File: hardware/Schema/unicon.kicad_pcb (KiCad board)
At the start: 2 copper layers, 31 x 45 mm, 72 parts, among them J1 PROG, J2 PWR, J3 SideA, J4 SideB, U1 LM340MP-5.0, U2 SIP21106-3.3, U3 STM32F051C8Tx, U4 AT24C16, Y1 8MHz, Y2 32768 Hz

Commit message: pcb paruosimas, schemos pataisymai
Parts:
- removed R22, R23: 47R, resistors:R_0805
- removed the REF** at (99.4, 113.2)
- added REF**: SolderWirePad_single_0-8mmDrill, Wire_Pads:SolderWirePad_single_0-8mmDrill, F.Cu at (107.0, 104.3)
- added REF**: Pin_Header_Straight_1x20_Pitch2.54mm, Pin_Headers:Pin_Header_Straight_1x20_Pitch2.54mm, F.Cu at (88.2, 154.0)
- added REF**: SolderWirePad_single_0-8mmDrill, Wire_Pads:SolderWirePad_single_0-8mmDrill, F.Cu at (99.8, 119.1)
- added REF**: SolderWirePad_single_0-8mmDrill, Wire_Pads:SolderWirePad_single_0-8mmDrill, F.Cu at (102.5, 124.8)
- added REF**: SolderWirePad_single_0-8mmDrill, Wire_Pads:SolderWirePad_single_0-8mmDrill, F.Cu at (107.8, 122.0)
- added REF**: SolderWirePad_single_0-8mmDrill, Wire_Pads:SolderWirePad_single_0-8mmDrill, F.Cu at (114.4, 118.9)
- added REF**: SolderWirePad_single_0-8mmDrill, Wire_Pads:SolderWirePad_single_0-8mmDrill, F.Cu at (117.7, 129.0)
- moved C4 17.3 mm to (111.3, 109.0), turned to 270 degrees
- moved R5 3.69 mm to (116.6, 117.7)
- moved R16 3.55 mm to (116.5, 107.2)
- moved R17 3.55 mm to (114.5, 107.2)
- moved REF** 2.31 mm to (118.1, 115.7)
- moved REF** 1.53 mm to (101.6, 103.2)
- moved REF** 1.43 mm to (104.5, 124.0)
- moved REF** 1.04 mm to (112.5, 135.3)
- moved REF** 1.00 mm to (113.6, 124.9)
- moved D1 0.95 mm to (107.2, 108.9)
- moved D9 0.80 mm to (101.5, 101.7)
- moved REF** 0.61 mm to (110.8, 122.1)
- moved RN3 0.30 mm to (99.8, 131.8)
- moved RN6 0.16 mm to (117.1, 121.5)
- moved RN7 0.16 mm to (117.1, 126.6)
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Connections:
- D3 pad 2: /5VDC -> /3VDC
- D4 pad 2: /5VDC -> /3VDC
- J1 pad 4: /~NRSTP -> /~NRST
- R16 pad 1: /ESCL -> /IO34
- R16 pad 2: /5VDC -> /3VDC
- R17 pad 1: /ESDA -> /IO35
- R17 pad 2: /5VDC -> /3VDC
- R5 pad 1: /~NRSTP -> /~NRST
- R5 pad 2: /~NRST -> /~NRSTP
- RN5 pad 3: (no net) -> Net-(RN5-Pad3)
- RN5 pad 5: (no net) -> Net-(RN5-Pad5)
- RN5 pad 7: (no net) -> Net-(RN5-Pad7)
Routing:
- net /3VDC: track 111.2 -> 137.9 mm
- net /~NRSTP: track 21.5 -> 3.45 mm, vias 1 -> 0
- net /~NRST: track 40.9 -> 46.6 mm
- net /5VDC: track 67.7 -> 62.8 mm, vias 3 -> 0
- net /ESDA: track 1.60 -> 0.00 mm
- net /ESCL: track 1.60 -> 0.00 mm
- net /IO35: track 44.5 -> 43.5 mm, vias 2 -> 0
- net /12VDC: track 5.07 -> 5.91 mm
- net Net-(D9-Pad1): track 4.47 -> 5.27 mm
- net /IO15: track 8.19 -> 8.72 mm
- net /IO34: vias 2 -> 4

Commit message: sugeneruoti gerberiai
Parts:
- removed the REF** at (88.2, 154.0)
- added C1: 100uFx16V, capacitors:CP_Radial_D5.0mm_P2.00mm, F.Cu at (167.3, 60.1)
- added C1: 100uFx16V, capacitors:CP_Radial_D5.0mm_P2.00mm, F.Cu at (135.3, 60.1)
- added C1: 100uFx16V, capacitors:CP_Radial_D5.0mm_P2.00mm, F.Cu at (103.3, 60.1)
- added C1: 100uFx16V, capacitors:CP_Radial_D5.0mm_P2.00mm, F.Cu at (167.3, 106.1)
- added C1: 100uFx16V, capacitors:CP_Radial_D5.0mm_P2.00mm, F.Cu at (135.3, 106.1)
- added C10: 100nF, capacitors:C_0805, B.Cu at (148.6, 54.3)
- added C10: 100nF, capacitors:C_0805, B.Cu at (180.6, 54.3)
- added C10: 100nF, capacitors:C_0805, B.Cu at (116.6, 54.3)
- added C10: 100nF, capacitors:C_0805, B.Cu at (180.6, 100.3)
- added C10: 100nF, capacitors:C_0805, B.Cu at (148.6, 100.3)
- added C11: 15pF, capacitors:C_0805, B.Cu at (165.0, 81.9)
- added C11: 15pF, capacitors:C_0805, B.Cu at (101.0, 81.9)
- added C11: 15pF, capacitors:C_0805, B.Cu at (133.0, 81.9)
- added C11: 15pF, capacitors:C_0805, B.Cu at (165.0, 127.9)
- added C11: 15pF, capacitors:C_0805, B.Cu at (133.0, 127.9)
- added C12: 15pF, capacitors:C_0805, B.Cu at (165.0, 80.4)
- added C12: 15pF, capacitors:C_0805, B.Cu at (101.0, 80.4)
- added C12: 15pF, capacitors:C_0805, B.Cu at (133.0, 80.4)
- added C12: 15pF, capacitors:C_0805, B.Cu at (165.0, 126.4)
- added C12: 15pF, capacitors:C_0805, B.Cu at (133.0, 126.4)
- added C13: 100nF, capacitors:C_0805, B.Cu at (152.6, 59.8)
- added C13: 100nF, capacitors:C_0805, B.Cu at (184.6, 59.8)
- added C13: 100nF, capacitors:C_0805, B.Cu at (120.6, 59.8)
- added C13: 100nF, capacitors:C_0805, B.Cu at (184.6, 105.8)
- added C13: 100nF, capacitors:C_0805, B.Cu at (152.6, 105.8)
- added C14: 100uFx16V, capacitors:CP_Radial_D5.0mm_P2.00mm, F.Cu at (183.3, 56.1)
- added C14: 100uFx16V, capacitors:CP_Radial_D5.0mm_P2.00mm, F.Cu at (151.3, 56.1)
- added C14: 100uFx16V, capacitors:CP_Radial_D5.0mm_P2.00mm, F.Cu at (119.3, 56.1)
- added C14: 100uFx16V, capacitors:CP_Radial_D5.0mm_P2.00mm, F.Cu at (183.3, 102.1)
- added C14: 100uFx16V, capacitors:CP_Radial_D5.0mm_P2.00mm, F.Cu at (151.3, 102.1)
- added C2: 100nF, capacitors:C_0805, F.Cu at (185.0, 64.8)
- added C2: 100nF, capacitors:C_0805, F.Cu at (153.0, 64.8)
- added C2: 100nF, capacitors:C_0805, F.Cu at (121.0, 64.8)
- added C2: 100nF, capacitors:C_0805, F.Cu at (185.0, 110.8)
- added C2: 100nF, capacitors:C_0805, F.Cu at (153.0, 110.8)
- added C20: 100nF, capacitors:C_0805, F.Cu at (177.7, 53.6)
- added C20: 100nF, capacitors:C_0805, F.Cu at (145.7, 53.6)
- added C20: 100nF, capacitors:C_0805, F.Cu at (113.7, 53.6)
- added C20: 100nF, capacitors:C_0805, F.Cu at (177.7, 99.6)
- added C20: 100nF, capacitors:C_0805, F.Cu at (145.7, 99.6)
- added C3: 100nF, capacitors:C_0805, F.Cu at (174.9, 72.8)
- added C3: 100nF, capacitors:C_0805, F.Cu at (110.9, 72.8)
- added C3: 100nF, capacitors:C_0805, F.Cu at (142.9, 72.8)
- added C3: 100nF, capacitors:C_0805, F.Cu at (174.9, 118.8)
- added C3: 100nF, capacitors:C_0805, F.Cu at (142.9, 118.8)
- added C4: 100nF, capacitors:C_0805, F.Cu at (175.3, 63.0)
- added C4: 100nF, capacitors:C_0805, F.Cu at (143.3, 63.0)
- added C4: 100nF, capacitors:C_0805, F.Cu at (111.3, 63.0)
- added C4: 100nF, capacitors:C_0805, F.Cu at (175.3, 109.0)
- added C4: 100nF, capacitors:C_0805, F.Cu at (143.3, 109.0)
- added C5: 15pF, capacitors:C_0805, B.Cu at (165.0, 83.5)
- added C5: 15pF, capacitors:C_0805, B.Cu at (101.0, 83.5)
- added C5: 15pF, capacitors:C_0805, B.Cu at (133.0, 83.5)
- added C5: 15pF, capacitors:C_0805, B.Cu at (165.0, 129.5)
- added C5: 15pF, capacitors:C_0805, B.Cu at (133.0, 129.5)
- added C6: 15pF, capacitors:C_0805, B.Cu at (165.0, 85.0)
- added C6: 15pF, capacitors:C_0805, B.Cu at (101.0, 85.0)
- added C6: 15pF, capacitors:C_0805, B.Cu at (133.0, 85.0)
- added C6: 15pF, capacitors:C_0805, B.Cu at (165.0, 131.0)
- added C6: 15pF, capacitors:C_0805, B.Cu at (133.0, 131.0)
- added C7: 100uFx16V, capacitors:CP_Radial_D5.0mm_P2.00mm, F.Cu at (164.5, 64.7)
- added C7: 100uFx16V, capacitors:CP_Radial_D5.0mm_P2.00mm, F.Cu at (132.5, 64.7)
- added C7: 100uFx16V, capacitors:CP_Radial_D5.0mm_P2.00mm, F.Cu at (100.5, 64.7)
- added C7: 100uFx16V, capacitors:CP_Radial_D5.0mm_P2.00mm, F.Cu at (164.5, 110.7)
- added C7: 100uFx16V, capacitors:CP_Radial_D5.0mm_P2.00mm, F.Cu at (132.5, 110.7)
- added C8: 100nF, capacitors:C_0805, F.Cu at (182.8, 61.3)
- added C8: 100nF, capacitors:C_0805, F.Cu at (150.8, 61.3)
- added C8: 100nF, capacitors:C_0805, F.Cu at (118.8, 61.3)
- added C8: 100nF, capacitors:C_0805, F.Cu at (182.8, 107.3)
- added C8: 100nF, capacitors:C_0805, F.Cu at (150.8, 107.3)
- added C9: 100nF, capacitors:C_0805, B.Cu at (146.7, 54.3)
- added C9: 100nF, capacitors:C_0805, B.Cu at (178.7, 54.3)
- added C9: 100nF, capacitors:C_0805, B.Cu at (114.7, 54.3)
- added C9: 100nF, capacitors:C_0805, B.Cu at (178.7, 100.3)
- added C9: 100nF, capacitors:C_0805, B.Cu at (146.7, 100.3)
- added D1: BAS32, disc:D_MiniMELF, F.Cu at (171.2, 62.9)
- added D1: BAS32, disc:D_MiniMELF, F.Cu at (139.2, 62.9)
- added D1: BAS32, disc:D_MiniMELF, F.Cu at (107.2, 62.9)
- added D1: BAS32, disc:D_MiniMELF, F.Cu at (171.2, 108.9)
- added D1: BAS32, disc:D_MiniMELF, F.Cu at (139.2, 108.9)
- added D2: LED1, disc:LED_0805, F.Cu at (167.8, 93.5)
- added D2: LED1, disc:LED_0805, F.Cu at (103.8, 93.5)
- added D2: LED1, disc:LED_0805, F.Cu at (135.8, 93.5)
- added D2: LED1, disc:LED_0805, F.Cu at (167.8, 139.5)
- added D2: LED1, disc:LED_0805, F.Cu at (135.8, 139.5)
- added D3: BAT54S, disc:SOT-23, F.Cu at (174.7, 53.6)
- added D3: BAT54S, disc:SOT-23, F.Cu at (142.7, 53.6)
- added D3: BAT54S, disc:SOT-23, F.Cu at (110.7, 53.6)
- added D3: BAT54S, disc:SOT-23, F.Cu at (174.7, 99.6)
- added D3: BAT54S, disc:SOT-23, F.Cu at (142.7, 99.6)
- added D4: BAT54S, disc:SOT-23, F.Cu at (171.1, 53.6)
- added D4: BAT54S, disc:SOT-23, F.Cu at (139.1, 53.6)
- added D4: BAT54S, disc:SOT-23, F.Cu at (107.1, 53.6)
- added D4: BAT54S, disc:SOT-23, F.Cu at (171.1, 99.6)
- added D4: BAT54S, disc:SOT-23, F.Cu at (139.1, 99.6)
- added D5: LED2, disc:LED_0805, F.Cu at (170.1, 93.5)
- added D5: LED2, disc:LED_0805, F.Cu at (106.1, 93.5)
- added D5: LED2, disc:LED_0805, F.Cu at (138.1, 93.5)
- added D5: LED2, disc:LED_0805, F.Cu at (170.1, 139.5)
- added D5: LED2, disc:LED_0805, F.Cu at (138.1, 139.5)
- added D6: LED1, disc:LED_0805, F.Cu at (175.9, 93.5)
- added D6: LED1, disc:LED_0805, F.Cu at (111.9, 93.5)
- added D6: LED1, disc:LED_0805, F.Cu at (143.9, 93.5)
- added D6: LED1, disc:LED_0805, F.Cu at (175.9, 139.5)
- added D6: LED1, disc:LED_0805, F.Cu at (143.9, 139.5)
- added D7: LED2, disc:LED_0805, F.Cu at (178.5, 93.5)
- added D7: LED2, disc:LED_0805, F.Cu at (114.5, 93.5)
- added D7: LED2, disc:LED_0805, F.Cu at (146.5, 93.5)
- added D7: LED2, disc:LED_0805, F.Cu at (178.5, 139.5)
- added D7: LED2, disc:LED_0805, F.Cu at (146.5, 139.5)
- added D8: 3V, disc:LED_0805, F.Cu at (185.0, 60.6)
- added D8: 3V, disc:LED_0805, F.Cu at (153.0, 60.6)
- added D8: 3V, disc:LED_0805, F.Cu at (121.0, 60.6)
- added D8: 3V, disc:LED_0805, F.Cu at (185.0, 106.6)
- added D8: 3V, disc:LED_0805, F.Cu at (153.0, 106.6)
- added D9: BAS32, disc:D_MiniMELF, F.Cu at (165.6, 55.7)
- added D9: BAS32, disc:D_MiniMELF, F.Cu at (133.6, 55.7)
- added D9: BAS32, disc:D_MiniMELF, F.Cu at (101.5, 55.7)
- added D9: BAS32, disc:D_MiniMELF, F.Cu at (165.6, 101.7)
- added D9: BAS32, disc:D_MiniMELF, F.Cu at (133.6, 101.7)
- added J1: PROG, mech:ISP_SWD_Connector, F.Cu at (168.8, 69.1)
- added J1: PROG, mech:ISP_SWD_Connector, F.Cu at (104.8, 69.1)
- added J1: PROG, mech:ISP_SWD_Connector, F.Cu at (136.8, 69.1)
- added J1: PROG, mech:ISP_SWD_Connector, F.Cu at (168.8, 115.1)
- added J1: PROG, mech:ISP_SWD_Connector, F.Cu at (136.8, 115.1)
- added J2: PWR, Pin_Headers:Pin_Header_Straight_2x03_Pitch2.54mm, F.Cu at (158.5, 56.9)
- added J2: PWR, Pin_Headers:Pin_Header_Straight_2x03_Pitch2.54mm, F.Cu at (126.5, 56.9)
- added J2: PWR, Pin_Headers:Pin_Header_Straight_2x03_Pitch2.54mm, F.Cu at (94.5, 56.9)
- added J2: PWR, Pin_Headers:Pin_Header_Straight_2x03_Pitch2.54mm, F.Cu at (158.5, 102.9)
- added J2: PWR, Pin_Headers:Pin_Header_Straight_2x03_Pitch2.54mm, F.Cu at (126.5, 102.9)
- added J3: SIDE A, Pin_Headers:Pin_Header_Straight_2x10_Pitch2.54mm, F.Cu at (158.5, 69.7)
- added J3: SIDE A, Pin_Headers:Pin_Header_Straight_2x10_Pitch2.54mm, F.Cu at (94.5, 69.7)
- added J3: SIDE A, Pin_Headers:Pin_Header_Straight_2x10_Pitch2.54mm, F.Cu at (126.5, 69.7)
- added J3: SIDE A, Pin_Headers:Pin_Header_Straight_2x10_Pitch2.54mm, F.Cu at (158.5, 115.7)
- added J3: SIDE A, Pin_Headers:Pin_Header_Straight_2x10_Pitch2.54mm, F.Cu at (126.5, 115.7)
- added J4: SIDE B, Pin_Headers:Pin_Header_Straight_2x10_Pitch2.54mm, F.Cu at (183.9, 69.7)
- added J4: SIDE B, Pin_Headers:Pin_Header_Straight_2x10_Pitch2.54mm, F.Cu at (151.9, 69.7)
- added J4: SIDE B, Pin_Headers:Pin_Header_Straight_2x10_Pitch2.54mm, F.Cu at (119.9, 69.7)
- added J4: SIDE B, Pin_Headers:Pin_Header_Straight_2x10_Pitch2.54mm, F.Cu at (183.9, 115.7)
- added J4: SIDE B, Pin_Headers:Pin_Header_Straight_2x10_Pitch2.54mm, F.Cu at (151.9, 115.7)
- added R1: 120R, resistors:R_0805, F.Cu at (176.9, 72.8)
- added R1: 120R, resistors:R_0805, F.Cu at (112.9, 72.8)
- added R1: 120R, resistors:R_0805, F.Cu at (144.9, 72.8)
- added R1: 120R, resistors:R_0805, F.Cu at (176.9, 118.8)
- added R1: 120R, resistors:R_0805, F.Cu at (144.9, 118.8)
- added R10: 120R, resistors:R_1206, F.Cu at (165.2, 53.4)
- added R10: 120R, resistors:R_1206, F.Cu at (133.2, 53.4)
- added R10: 120R, resistors:R_1206, F.Cu at (101.2, 53.4)
- added R10: 120R, resistors:R_1206, F.Cu at (165.2, 99.4)
- added R10: 120R, resistors:R_1206, F.Cu at (133.2, 99.4)
- added R16: 4.7k, resistors:R_0805, F.Cu at (180.5, 61.2)
- added R16: 4.7k, resistors:R_0805, F.Cu at (148.5, 61.2)
- added R16: 4.7k, resistors:R_0805, F.Cu at (116.5, 61.2)
- added R16: 4.7k, resistors:R_0805, F.Cu at (180.5, 107.2)
- added R16: 4.7k, resistors:R_0805, F.Cu at (148.5, 107.2)
- added R17: 4.7k, resistors:R_0805, F.Cu at (178.5, 61.2)
- added R17: 4.7k, resistors:R_0805, F.Cu at (146.5, 61.2)
- added R17: 4.7k, resistors:R_0805, F.Cu at (114.5, 61.2)
- added R17: 4.7k, resistors:R_0805, F.Cu at (178.5, 107.2)
- added R17: 4.7k, resistors:R_0805, F.Cu at (146.5, 107.2)
- added R2: 10k, resistors:R_0805, F.Cu at (172.9, 72.8)
- added R2: 10k, resistors:R_0805, F.Cu at (108.9, 72.8)
- added R2: 10k, resistors:R_0805, F.Cu at (140.9, 72.8)
- added R2: 10k, resistors:R_0805, F.Cu at (172.9, 118.8)
- added R2: 10k, resistors:R_0805, F.Cu at (140.9, 118.8)
- added R3: 47R, resistors:R_0805, F.Cu at (168.9, 72.8)
- added R3: 47R, resistors:R_0805, F.Cu at (104.9, 72.8)
- added R3: 47R, resistors:R_0805, F.Cu at (136.9, 72.8)
- added R3: 47R, resistors:R_0805, F.Cu at (168.9, 118.8)
- added R3: 47R, resistors:R_0805, F.Cu at (136.9, 118.8)
- added R32: 10k, resistors:R_0805, F.Cu at (178.5, 57.3)
- added R32: 10k, resistors:R_0805, F.Cu at (146.5, 57.3)
- added R32: 10k, resistors:R_0805, F.Cu at (114.5, 57.3)
- added R32: 10k, resistors:R_0805, F.Cu at (178.5, 103.3)
- added R32: 10k, resistors:R_0805, F.Cu at (146.5, 103.3)
- added R4: 47R, resistors:R_0805, F.Cu at (170.9, 72.8)
- added R4: 47R, resistors:R_0805, F.Cu at (106.9, 72.8)
- added R4: 47R, resistors:R_0805, F.Cu at (138.9, 72.8)
- added R4: 47R, resistors:R_0805, F.Cu at (170.9, 118.8)
- added R4: 47R, resistors:R_0805, F.Cu at (138.9, 118.8)
- added R5: 47R, resistors:R_0805, F.Cu at (180.6, 71.7)
- added R5: 47R, resistors:R_0805, F.Cu at (116.6, 71.7)
- added R5: 47R, resistors:R_0805, F.Cu at (148.6, 71.7)
- added R5: 47R, resistors:R_0805, F.Cu at (180.6, 117.7)
- added R5: 47R, resistors:R_0805, F.Cu at (148.6, 117.7)
- added R6: 15k, resistors:R_0805, F.Cu at (180.6, 68.6)
- added R6: 15k, resistors:R_0805, F.Cu at (116.6, 68.6)
- added R6: 15k, resistors:R_0805, F.Cu at (148.6, 68.6)
- added R6: 15k, resistors:R_0805, F.Cu at (180.6, 114.6)
- added R6: 15k, resistors:R_0805, F.Cu at (148.6, 114.6)
- added R7: 120R, resistors:R_0805, F.Cu at (182.8, 64.8)
- added R7: 120R, resistors:R_0805, F.Cu at (150.8, 64.8)
- added R7: 120R, resistors:R_0805, F.Cu at (118.8, 64.8)
- added R7: 120R, resistors:R_0805, F.Cu at (182.8, 110.8)
- added R7: 120R, resistors:R_0805, F.Cu at (150.8, 110.8)
- added R8: 15k, resistors:R_0805, B.Cu at (146.7, 59.8)
- added R8: 15k, resistors:R_0805, B.Cu at (178.7, 59.8)
- added R8: 15k, resistors:R_0805, B.Cu at (114.7, 59.8)
- added R8: 15k, resistors:R_0805, B.Cu at (178.7, 105.8)
- added R8: 15k, resistors:R_0805, B.Cu at (146.7, 105.8)
- added R9: 1M2, resistors:R_0805, B.Cu at (165.0, 86.5)
- added R9: 1M2, resistors:R_0805, B.Cu at (101.0, 86.5)
- added R9: 1M2, resistors:R_0805, B.Cu at (133.0, 86.5)
- added R9: 1M2, resistors:R_0805, B.Cu at (165.0, 132.5)
- added R9: 1M2, resistors:R_0805, B.Cu at (133.0, 132.5)
- added REF**: SolderWirePad_single_0-8mmDrill, Wire_Pads:SolderWirePad_single_0-8mmDrill, F.Cu at (182.1, 69.7)
- added REF**: SolderWirePad_single_0-8mmDrill, Wire_Pads:SolderWirePad_single_0-8mmDrill, F.Cu at (166.9, 79.0)
- added REF**: SolderWirePad_single_0-8mmDrill, Wire_Pads:SolderWirePad_single_0-8mmDrill, F.Cu at (163.7, 94.3)
- added REF**: SolderWirePad_single_0-8mmDrill, Wire_Pads:SolderWirePad_single_0-8mmDrill, F.Cu at (171.8, 76.0)
- added REF**: SolderWirePad_single_0-8mmDrill, Wire_Pads:SolderWirePad_single_0-8mmDrill, F.Cu at (174.3, 76.1)
- added REF**: SolderWirePad_single_0-8mmDrill, Wire_Pads:SolderWirePad_single_0-8mmDrill, F.Cu at (174.9, 82.0)
- added REF**: SolderWirePad_single_0-8mmDrill, Wire_Pads:SolderWirePad_single_0-8mmDrill, F.Cu at (173.5, 86.1)
- added REF**: SolderWirePad_single_0-8mmDrill, Wire_Pads:SolderWirePad_single_0-8mmDrill, F.Cu at (176.5, 89.3)
- added REF**: SolderWirePad_single_0-8mmDrill, Wire_Pads:SolderWirePad_single_0-8mmDrill, F.Cu at (177.6, 78.9)
- added REF**: SolderWirePad_single_0-8mmDrill, Wire_Pads:SolderWirePad_single_0-8mmDrill, F.Cu at (168.5, 78.0)
- added REF**: SolderWirePad_single_0-8mmDrill, Wire_Pads:SolderWirePad_single_0-8mmDrill, F.Cu at (148.1, 57.2)
- added REF**: SolderWirePad_single_0-8mmDrill, Wire_Pads:SolderWirePad_single_0-8mmDrill, F.Cu at (166.5, 62.7)
- added REF**: SolderWirePad_single_0-8mmDrill, Wire_Pads:SolderWirePad_single_0-8mmDrill, F.Cu at (134.5, 62.7)
- added REF**: SolderWirePad_single_0-8mmDrill, Wire_Pads:SolderWirePad_single_0-8mmDrill, F.Cu at (133.6, 57.2)
- added REF**: SolderWirePad_single_0-8mmDrill, Wire_Pads:SolderWirePad_single_0-8mmDrill, F.Cu at (139.0, 58.3)
- added REF**: SolderWirePad_single_0-8mmDrill, Wire_Pads:SolderWirePad_single_0-8mmDrill, F.Cu at (99.7, 94.3)
- added REF**: SolderWirePad_single_0-8mmDrill, Wire_Pads:SolderWirePad_single_0-8mmDrill, F.Cu at (112.5, 89.3)
- added REF**: SolderWirePad_single_0-8mmDrill, Wire_Pads:SolderWirePad_single_0-8mmDrill, F.Cu at (110.9, 82.0)
- added REF**: SolderWirePad_single_0-8mmDrill, Wire_Pads:SolderWirePad_single_0-8mmDrill, F.Cu at (109.5, 86.1)
- added REF**: SolderWirePad_single_0-8mmDrill, Wire_Pads:SolderWirePad_single_0-8mmDrill, F.Cu at (104.5, 78.0)
- added REF**: SolderWirePad_single_0-8mmDrill, Wire_Pads:SolderWirePad_single_0-8mmDrill, F.Cu at (102.9, 79.0)
- added REF**: SolderWirePad_single_0-8mmDrill, Wire_Pads:SolderWirePad_single_0-8mmDrill, F.Cu at (113.6, 78.9)
- added REF**: SolderWirePad_single_0-8mmDrill, Wire_Pads:SolderWirePad_single_0-8mmDrill, F.Cu at (165.6, 57.2)
- added REF**: SolderWirePad_single_0-8mmDrill, Wire_Pads:SolderWirePad_single_0-8mmDrill, F.Cu at (107.8, 76.0)
- added REF**: SolderWirePad_single_0-8mmDrill, Wire_Pads:SolderWirePad_single_0-8mmDrill, F.Cu at (99.8, 73.1)
- added REF**: SolderWirePad_single_0-8mmDrill, Wire_Pads:SolderWirePad_single_0-8mmDrill, F.Cu at (102.5, 62.7)
- added REF**: SolderWirePad_single_0-8mmDrill, Wire_Pads:SolderWirePad_single_0-8mmDrill, F.Cu at (101.6, 57.2)
- added REF**: SolderWirePad_single_0-8mmDrill, Wire_Pads:SolderWirePad_single_0-8mmDrill, F.Cu at (110.3, 76.1)
- added REF**: SolderWirePad_single_0-8mmDrill, Wire_Pads:SolderWirePad_single_0-8mmDrill, F.Cu at (114.4, 72.9)
- added REF**: SolderWirePad_single_0-8mmDrill, Wire_Pads:SolderWirePad_single_0-8mmDrill, F.Cu at (107.0, 58.3)
- added REF**: SolderWirePad_single_0-8mmDrill, Wire_Pads:SolderWirePad_single_0-8mmDrill, F.Cu at (116.1, 57.2)
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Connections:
- net /IO1 renamed /A0
- net /IO10 renamed /B0
- net /IO11 renamed /B1
- net /IO12 renamed /B2
- net /IO13 renamed /B8
- net /IO14 renamed /B9
- net /IO15 renamed /C13
- net /IO16 renamed /B10
- net /IO17 renamed /B11
- net /IO18 renamed /B14
- net /IO19 renamed /B15
- net /IO2 renamed /A1
- net /IO20 renamed /A8
- net /IO21 renamed /F7
- net /IO22 renamed /A15
- net /IO23 renamed /B3
- net /IO24 renamed /B4
- net /IO25 renamed /B5
- net /IO26 renamed /A5
- net /IO27 renamed /A6
- net /IO28 renamed /A7
- net /IO29 renamed /A9
- net /IO3 renamed /A2
- net /IO30 renamed /A10
- net /IO31 renamed /A11
- net /IO32 renamed /A12
- net /IO33 renamed /F6
- net /IO34 renamed /B6
- net /IO35 renamed /B7
- net /IO36 renamed /B12
- net /IO37 renamed /B13
- net /IO4 renamed /A3
- net /IO9 renamed /A4
- net Net-(J3-Pad10) renamed /PA5
- net Net-(J3-Pad11) renamed /PA6
- net Net-(J3-Pad12) renamed /PA7
- net Net-(J3-Pad13) renamed /PA0
- net Net-(J3-Pad14) renamed /PA1
- net Net-(J3-Pad15) renamed /PA2
- net Net-(J3-Pad16) renamed /PA3
- net Net-(J3-Pad17) renamed /PB0
- net Net-(J3-Pad18) renamed /PB1
- net Net-(J3-Pad19) renamed /PB2
- net Net-(J3-Pad20) renamed /PB10
- net Net-(J3-Pad4) renamed /PB6
- net Net-(J3-Pad5) renamed /PB7
- net Net-(J3-Pad6) renamed /PB8
- net Net-(J3-Pad7) renamed /PB9
- net Net-(J3-Pad8) renamed /PC13
- net Net-(J3-Pad9) renamed /PA4
- net Net-(J4-Pad10) renamed /PF7
- net Net-(J4-Pad11) renamed /PA11
- net Net-(J4-Pad12) renamed /PA12
- net Net-(J4-Pad13) renamed /PA9
- net Net-(J4-Pad14) renamed /PA10
- net Net-(J4-Pad15) renamed /PB15
- net Net-(J4-Pad16) renamed /PA8
- net Net-(J4-Pad17) renamed /PB13
- net Net-(J4-Pad18) renamed /PB14
- net Net-(J4-Pad19) renamed /PB11
- net Net-(J4-Pad20) renamed /PB12
- net Net-(J4-Pad5) renamed /PB4
- net Net-(J4-Pad6) renamed /PB5
- net Net-(J4-Pad7) renamed /PA15
- net Net-(J4-Pad8) renamed /PB3
- net Net-(J4-Pad9) renamed /PF6
- C3 pad 1: /BOOT0 -> /BT0
- J4 pad 4: /BOOTA -> /BOOT0
- R1 pad 1: /BOOT0 -> /BT0
- R1 pad 2: /BOOTA -> /BOOT0
- R2 pad 2: /BOOT0 -> /BT0
- RN5 pad 3: Net-(RN5-Pad3) -> (no net)
- RN5 pad 5: Net-(RN5-Pad5) -> (no net)
- RN5 pad 7: Net-(RN5-Pad7) -> (no net)
- U3 pad 44: /BOOT0 -> /BT0
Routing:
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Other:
- board size 31 x 45 mm -> 95 x 91 mm

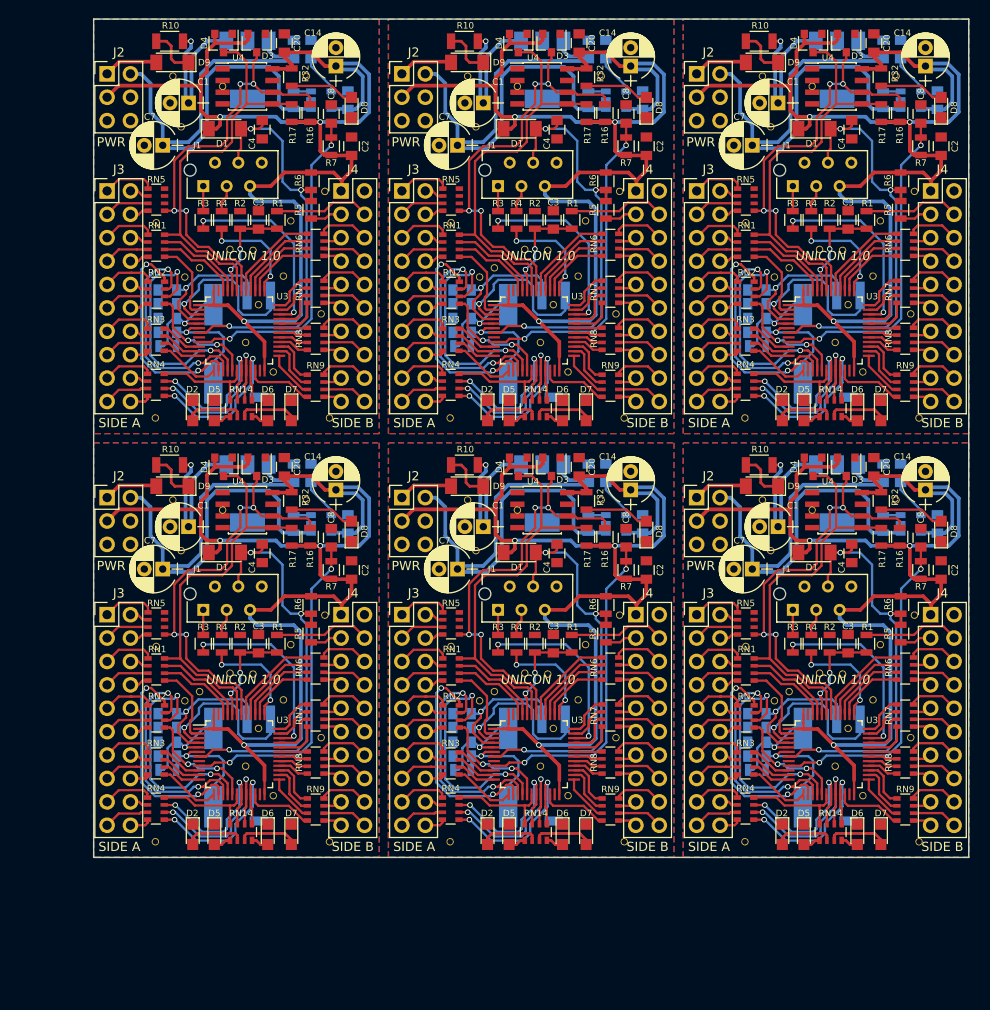
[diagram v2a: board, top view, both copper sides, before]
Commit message: vbat atjungtas nuo 3vdc ir isvestas i J1 jungti
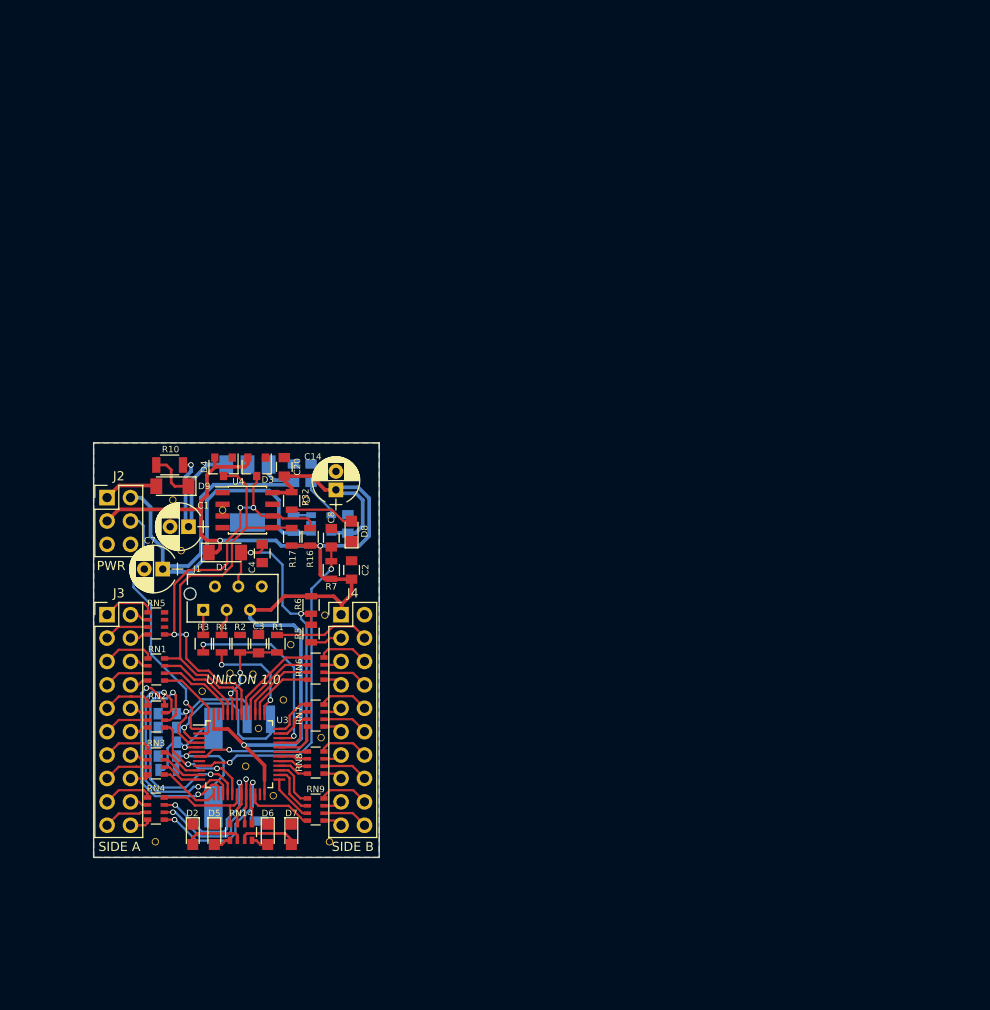
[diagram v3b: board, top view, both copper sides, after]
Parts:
- removed the C1 at (167.3, 60.1)
- removed the C1 at (135.3, 60.1)
- removed the C1 at (103.3, 60.1)
- removed the C1 at (167.3, 106.1)
- removed the C1 at (135.3, 106.1)
- removed the C10 at (148.6, 54.3)
- removed the C10 at (180.6, 54.3)
- removed the C10 at (116.6, 54.3)
- removed the C10 at (180.6, 100.3)
- removed the C10 at (148.6, 100.3)
- removed the C11 at (165.0, 81.9)
- removed the C11 at (101.0, 81.9)
- removed the C11 at (133.0, 81.9)
- removed the C11 at (165.0, 127.9)
- removed the C11 at (133.0, 127.9)
- removed the C12 at (165.0, 80.4)
- removed the C12 at (101.0, 80.4)
- removed the C12 at (133.0, 80.4)
- removed the C12 at (165.0, 126.4)
- removed the C12 at (133.0, 126.4)
- removed the C13 at (152.6, 59.8)
- removed the C13 at (184.6, 59.8)
- removed the C13 at (120.6, 59.8)
- removed the C13 at (184.6, 105.8)
- removed the C13 at (152.6, 105.8)
- removed the C14 at (183.3, 56.1)
- removed the C14 at (151.3, 56.1)
- removed the C14 at (119.3, 56.1)
- removed the C14 at (183.3, 102.1)
- removed the C14 at (151.3, 102.1)
- removed the C2 at (185.0, 64.8)
- removed the C2 at (153.0, 64.8)
- removed the C2 at (121.0, 64.8)
- removed the C2 at (185.0, 110.8)
- removed the C2 at (153.0, 110.8)
- removed the C20 at (177.7, 53.6)
- removed the C20 at (145.7, 53.6)
- removed the C20 at (113.7, 53.6)
- removed the C20 at (177.7, 99.6)
- removed the C20 at (145.7, 99.6)
- removed the C3 at (174.9, 72.8)
- removed the C3 at (110.9, 72.8)
- removed the C3 at (142.9, 72.8)
- removed the C3 at (174.9, 118.8)
- removed the C3 at (142.9, 118.8)
- removed the C4 at (175.3, 63.0)
- removed the C4 at (143.3, 63.0)
- removed the C4 at (111.3, 63.0)
- removed the C4 at (175.3, 109.0)
- removed the C4 at (143.3, 109.0)
- removed the C5 at (165.0, 83.5)
- removed the C5 at (101.0, 83.5)
- removed the C5 at (133.0, 83.5)
- removed the C5 at (165.0, 129.5)
- removed the C5 at (133.0, 129.5)
- removed the C6 at (165.0, 85.0)
- removed the C6 at (101.0, 85.0)
- removed the C6 at (133.0, 85.0)
- removed the C6 at (165.0, 131.0)
- removed the C6 at (133.0, 131.0)
- removed the C7 at (164.5, 64.7)
- removed the C7 at (132.5, 64.7)
- removed the C7 at (100.5, 64.7)
- removed the C7 at (164.5, 110.7)
- removed the C7 at (132.5, 110.7)
- removed the C8 at (182.8, 61.3)
- removed the C8 at (150.8, 61.3)
- removed the C8 at (118.8, 61.3)
- removed the C8 at (182.8, 107.3)
- removed the C8 at (150.8, 107.3)
- removed the C9 at (146.7, 54.3)
- removed the C9 at (178.7, 54.3)
- removed the C9 at (114.7, 54.3)
- removed the C9 at (178.7, 100.3)
- removed the C9 at (146.7, 100.3)
- removed the D1 at (171.2, 62.9)
- removed the D1 at (139.2, 62.9)
- removed the D1 at (107.2, 62.9)
- removed the D1 at (171.2, 108.9)
- removed the D1 at (139.2, 108.9)
- removed the D2 at (167.8, 93.5)
- removed the D2 at (103.8, 93.5)
- removed the D2 at (135.8, 93.5)
- removed the D2 at (167.8, 139.5)
- removed the D2 at (135.8, 139.5)
- removed the D3 at (174.7, 53.6)
- removed the D3 at (142.7, 53.6)
- removed the D3 at (110.7, 53.6)
- removed the D3 at (174.7, 99.6)
- removed the D3 at (142.7, 99.6)
- removed the D4 at (171.1, 53.6)
- removed the D4 at (139.1, 53.6)
- removed the D4 at (107.1, 53.6)
- removed the D4 at (171.1, 99.6)
- removed the D4 at (139.1, 99.6)
- removed the D5 at (170.1, 93.5)
- removed the D5 at (106.1, 93.5)
- removed the D5 at (138.1, 93.5)
- removed the D5 at (170.1, 139.5)
- removed the D5 at (138.1, 139.5)
- removed the D6 at (175.9, 93.5)
- removed the D6 at (111.9, 93.5)
- removed the D6 at (143.9, 93.5)
- removed the D6 at (175.9, 139.5)
- removed the D6 at (143.9, 139.5)
- removed the D7 at (178.5, 93.5)
- removed the D7 at (114.5, 93.5)
- removed the D7 at (146.5, 93.5)
- removed the D7 at (178.5, 139.5)
- removed the D7 at (146.5, 139.5)
- removed the D8 at (185.0, 60.6)
- removed the D8 at (153.0, 60.6)
- removed the D8 at (121.0, 60.6)
- removed the D8 at (185.0, 106.6)
- removed the D8 at (153.0, 106.6)
- removed the D9 at (165.6, 55.7)
- removed the D9 at (133.6, 55.7)
- removed the D9 at (101.5, 55.7)
- removed the D9 at (165.6, 101.7)
- removed the D9 at (133.6, 101.7)
- removed the J1 at (168.8, 69.1)
- removed the J1 at (104.8, 69.1)
- removed the J1 at (136.8, 69.1)
- removed the J1 at (168.8, 115.1)
- removed the J1 at (136.8, 115.1)
- removed the J2 at (158.5, 56.9)
- removed the J2 at (126.5, 56.9)
- removed the J2 at (94.5, 56.9)
- removed the J2 at (158.5, 102.9)
- removed the J2 at (126.5, 102.9)
- removed the J3 at (158.5, 69.7)
- removed the J3 at (94.5, 69.7)
- removed the J3 at (126.5, 69.7)
- removed the J3 at (158.5, 115.7)
- removed the J3 at (126.5, 115.7)
- removed the J4 at (183.9, 69.7)
- removed the J4 at (151.9, 69.7)
- removed the J4 at (119.9, 69.7)
- removed the J4 at (183.9, 115.7)
- removed the J4 at (151.9, 115.7)
- removed the R1 at (176.9, 72.8)
- removed the R1 at (112.9, 72.8)
- removed the R1 at (144.9, 72.8)
- removed the R1 at (176.9, 118.8)
- removed the R1 at (144.9, 118.8)
- removed the R10 at (165.2, 53.4)
- removed the R10 at (133.2, 53.4)
- removed the R10 at (101.2, 53.4)
- removed the R10 at (165.2, 99.4)
- removed the R10 at (133.2, 99.4)
- removed the R16 at (180.5, 61.2)
- removed the R16 at (148.5, 61.2)
- removed the R16 at (116.5, 61.2)
- removed the R16 at (180.5, 107.2)
- removed the R16 at (148.5, 107.2)
- removed the R17 at (178.5, 61.2)
- removed the R17 at (146.5, 61.2)
- removed the R17 at (114.5, 61.2)
- removed the R17 at (178.5, 107.2)
- removed the R17 at (146.5, 107.2)
- removed the R2 at (172.9, 72.8)
- removed the R2 at (108.9, 72.8)
- removed the R2 at (140.9, 72.8)
- removed the R2 at (172.9, 118.8)
- removed the R2 at (140.9, 118.8)
- removed the R3 at (168.9, 72.8)
- removed the R3 at (104.9, 72.8)
- removed the R3 at (136.9, 72.8)
- removed the R3 at (168.9, 118.8)
- removed the R3 at (136.9, 118.8)
- removed the R32 at (178.5, 57.3)
- removed the R32 at (146.5, 57.3)
- removed the R32 at (114.5, 57.3)
- removed the R32 at (178.5, 103.3)
- removed the R32 at (146.5, 103.3)
- removed the R4 at (170.9, 72.8)
- removed the R4 at (106.9, 72.8)
- removed the R4 at (138.9, 72.8)
- removed the R4 at (170.9, 118.8)
- removed the R4 at (138.9, 118.8)
- removed the R5 at (180.6, 71.7)
- removed the R5 at (116.6, 71.7)
- removed the R5 at (148.6, 71.7)
- removed the R5 at (180.6, 117.7)
- removed the R5 at (148.6, 117.7)
- removed the R6 at (180.6, 68.6)
- removed the R6 at (116.6, 68.6)
- removed the R6 at (148.6, 68.6)
- removed the R6 at (180.6, 114.6)
- removed the R6 at (148.6, 114.6)
- removed the R7 at (182.8, 64.8)
- removed the R7 at (150.8, 64.8)
- removed the R7 at (118.8, 64.8)
- removed the R7 at (182.8, 110.8)
- removed the R7 at (150.8, 110.8)
- removed the R8 at (146.7, 59.8)
- removed the R8 at (178.7, 59.8)
- removed the R8 at (114.7, 59.8)
- removed the R8 at (178.7, 105.8)
- removed the R8 at (146.7, 105.8)
- removed the R9 at (165.0, 86.5)
- removed the R9 at (101.0, 86.5)
- removed the R9 at (133.0, 86.5)
- removed the R9 at (165.0, 132.5)
- removed the R9 at (133.0, 132.5)
- removed the REF** at (182.1, 69.7)
- removed the REF** at (166.9, 79.0)
- removed the REF** at (163.7, 94.3)
- removed the REF** at (171.8, 76.0)
- removed the REF** at (174.3, 76.1)
- removed the REF** at (174.9, 82.0)
- removed the REF** at (173.5, 86.1)
- removed the REF** at (176.5, 89.3)
- removed the REF** at (177.6, 78.9)
- removed the REF** at (168.5, 78.0)
- removed the REF** at (148.1, 57.2)
- removed the REF** at (166.5, 62.7)
- removed the REF** at (134.5, 62.7)
- removed the REF** at (133.6, 57.2)
- removed the REF** at (139.0, 58.3)
- removed the REF** at (99.7, 94.3)
- removed the REF** at (112.5, 89.3)
- removed the REF** at (110.9, 82.0)
- removed the REF** at (109.5, 86.1)
- removed the REF** at (104.5, 78.0)
- removed the REF** at (102.9, 79.0)
- removed the REF** at (113.6, 78.9)
- removed the REF** at (165.6, 57.2)
- removed the REF** at (107.8, 76.0)
- removed the REF** at (99.8, 73.1)
- removed the REF** at (102.5, 62.7)
- removed the REF** at (101.6, 57.2)
- removed the REF** at (110.3, 76.1)
- removed the REF** at (114.4, 72.9)
- removed the REF** at (107.0, 58.3)
- removed the REF** at (116.1, 57.2)
- removed the REF** at (118.1, 69.7)
- removed the REF** at (150.1, 69.7)
- removed the REF** at (171.0, 58.3)
- removed the REF** at (146.4, 72.9)
- removed the REF** at (136.5, 78.0)
- removed the REF** at (134.9, 79.0)
- removed the REF** at (131.8, 73.1)
- removed the REF** at (145.6, 78.9)
- removed the REF** at (142.9, 82.0)
- removed the REF** at (142.3, 76.1)
- removed the REF** at (139.8, 76.0)
- removed the REF** at (149.7, 83.0)
- removed the REF** at (150.6, 94.3)
- removed the REF** at (180.1, 57.2)
- removed the REF** at (131.7, 94.3)
- removed the REF** at (118.6, 94.3)
- removed the REF** at (117.7, 83.0)
- removed the REF** at (141.5, 86.1)
- removed the REF** at (144.5, 89.3)
- removed the REF** at (180.1, 103.2)
- removed the REF** at (165.6, 103.2)
- removed the REF** at (166.5, 108.7)
- removed the REF** at (171.0, 104.3)
- removed the REF** at (174.3, 122.1)
- removed the REF** at (163.8, 73.1)
- removed the REF** at (171.8, 122.0)
- removed the REF** at (178.4, 118.9)
- removed the REF** at (182.1, 115.7)
- removed the REF** at (182.6, 140.3)
- removed the REF** at (181.7, 129.0)
- removed the REF** at (173.5, 132.1)
- removed the REF** at (177.6, 124.9)
- removed the REF** at (176.5, 135.3)
- removed the REF** at (168.5, 124.0)
- removed the REF** at (166.9, 125.0)
- removed the REF** at (178.4, 72.9)
- removed the REF** at (174.9, 128.0)
- removed the REF** at (163.8, 119.1)
- removed the REF** at (163.7, 140.3)
- removed the REF** at (148.1, 103.2)
- removed the REF** at (133.6, 103.2)
- removed the REF** at (134.5, 108.7)
- removed the REF** at (139.0, 104.3)
- removed the REF** at (142.3, 122.1)
- removed the REF** at (139.8, 122.0)
- removed the REF** at (146.4, 118.9)
- removed the REF** at (182.6, 94.3)
- removed the REF** at (150.1, 115.7)
- removed the REF** at (150.6, 140.3)
- removed the REF** at (149.7, 129.0)
- removed the REF** at (141.5, 132.1)
- removed the REF** at (145.6, 124.9)
- removed the REF** at (144.5, 135.3)
- removed the REF** at (136.5, 124.0)
- removed the REF** at (134.9, 125.0)
- removed the REF** at (142.9, 128.0)
- removed the REF** at (131.8, 119.1)
- removed the REF** at (181.7, 83.0)
- removed the REF** at (131.7, 140.3)
- removed the REF** at (99.8, 119.1)
- removed the REF** at (102.9, 125.0)
- removed the RN1 at (163.8, 75.6)
- removed the RN1 at (99.8, 75.6)
- removed the RN1 at (131.8, 75.6)
- removed the RN1 at (163.8, 121.6)
- removed the RN1 at (131.8, 121.6)
- removed the RN14 at (173.0, 93.2)
- removed the RN14 at (109.0, 93.2)
- removed the RN14 at (141.0, 93.2)
- removed the RN14 at (173.0, 139.2)
- removed the RN14 at (141.0, 139.2)
- removed the RN2 at (163.8, 80.7)
- removed the RN2 at (99.8, 80.7)
- removed the RN2 at (131.8, 80.7)
- removed the RN2 at (163.8, 126.7)
- removed the RN2 at (131.8, 126.7)
- removed the RN3 at (163.8, 85.8)
- removed the RN3 at (99.8, 85.8)
- removed the RN3 at (131.8, 85.8)
- removed the RN3 at (163.8, 131.8)
- removed the RN3 at (131.8, 131.8)
- removed the RN4 at (163.8, 90.7)
- removed the RN4 at (99.8, 90.7)
- removed the RN4 at (131.8, 90.7)
- removed the RN4 at (163.8, 136.7)
- removed the RN4 at (131.8, 136.7)
- removed the RN5 at (163.8, 70.6)
- removed the RN5 at (99.8, 70.6)
- removed the RN5 at (131.8, 70.6)
- removed the RN5 at (163.8, 116.6)
- removed the RN5 at (131.8, 116.6)
- removed the RN6 at (181.1, 75.5)
- removed the RN6 at (117.1, 75.5)
- removed the RN6 at (149.1, 75.5)
- removed the RN6 at (181.1, 121.5)
- removed the RN6 at (149.1, 121.5)
- removed the RN7 at (181.1, 80.6)
- removed the RN7 at (117.1, 80.6)
- removed the RN7 at (149.1, 80.6)
- removed the RN7 at (181.1, 126.6)
- removed the RN7 at (149.1, 126.6)
- removed the RN8 at (181.1, 85.7)
- removed the RN8 at (149.1, 85.7)
- removed the RN8 at (117.1, 85.7)
- removed the RN8 at (181.1, 131.7)
- removed the RN8 at (149.1, 131.7)
- removed the RN9 at (181.1, 90.8)
- removed the RN9 at (117.1, 90.8)
- removed the RN9 at (149.1, 90.8)
- removed the RN9 at (181.1, 136.8)
- removed the RN9 at (149.1, 136.8)
- removed the U1 at (141.7, 56.5)
- removed the U1 at (173.7, 56.5)
- removed the U1 at (109.7, 56.5)
- removed the U1 at (173.7, 102.5)
- removed the U1 at (141.7, 102.5)
- removed the U2 at (149.7, 59.8)
- removed the U2 at (181.7, 59.8)
- removed the U2 at (117.7, 59.8)
- removed the U2 at (181.7, 105.8)
- removed the U2 at (149.7, 105.8)
- removed the U3 at (172.8, 84.8)
- removed the U3 at (108.8, 84.8)
- removed the U3 at (140.8, 84.8)
- removed the U3 at (172.8, 130.8)
- removed the U3 at (140.8, 130.8)
- removed the U4 at (173.7, 58.3)
- removed the U4 at (141.7, 58.3)
- removed the U4 at (109.7, 58.3)
- removed the U4 at (173.7, 104.3)
- removed the U4 at (141.7, 104.3)
- removed the Y1 at (170.0, 86.2)
- removed the Y1 at (106.0, 86.2)
- removed the Y1 at (138.0, 86.2)
- removed the Y1 at (170.0, 132.2)
- removed the Y1 at (138.0, 132.2)
- removed the Y2 at (176.2, 81.0)
- removed the Y2 at (112.2, 81.0)
- removed the Y2 at (144.2, 81.0)
- removed the Y2 at (176.2, 127.0)
- removed the Y2 at (144.2, 127.0)
- moved REF** 0.28 mm to (104.8, 124.0)
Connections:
- J2 pad 4: /COM -> /VBAT
- RN5 pad 3: (no net) -> Net-(RN5-Pad3)
- RN5 pad 5: (no net) -> Net-(RN5-Pad5)
- RN5 pad 7: (no net) -> Net-(RN5-Pad7)
- U3 pad 1: /3VDC -> /VBAT
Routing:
- net /3VDC: track 827.5 -> 136.3 mm, vias 18 -> 3
- net /5VDC: track 376.7 -> 62.8 mm
- net /~NRST: track 279.5 -> 46.6 mm, vias 18 -> 3
- net /B6: track 277.8 -> 46.3 mm, vias 24 -> 4
- net /B7: track 261.1 -> 43.5 mm
- net /VDDA: track 212.2 -> 35.4 mm, vias 12 -> 2
- net /A6: track 155.6 -> 26.2 mm, vias 12 -> 2
- net /A5: track 148.6 -> 25.0 mm, vias 12 -> 2
- net /A4: track 143.2 -> 23.9 mm, vias 12 -> 2
- net /SWDIO: track 125.3 -> 20.9 mm, vias 12 -> 2
- net /B10: track 119.8 -> 20.0 mm, vias 12 -> 2
- net /B2: track 119.1 -> 19.9 mm, vias 12 -> 2
- net /OSC32_I: track 113.5 -> 18.9 mm, vias 6 -> 1
- net /B1: track 111.2 -> 18.5 mm, vias 12 -> 2
- net Net-(C1-Pad1): track 105.8 -> 17.6 mm, vias 6 -> 1
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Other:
- board size 95 x 91 mm -> 31 x 45 mm
- board text added: "1"
- board text added: "10"
- board text added: "11"
- board text added: "12"
- board text added: "12VDC"
- board text added: "13"
- board text added: "14"
- board text added: "15"
- board text added: "16"
- board text added: "17"
- board text added: "18"
- board text added: "19"
- board text added: "2"
- board text added: "20"
- board text added: "3"
- board text added: "3VDC"
- board text added: "4"
- board text added: "5"
- board text added: "5VDC"
- board text added: "6"
- board text added: "7"
- board text added: "8"
- board text added: "9"
- board text added: "BOOT0"
- board text added: "COM"
- board text added: "J1"
- board text added: "J2"
- board text added: "J3"
- board text added: "J4"
- board text added: "NC"
- board text added: "PA0"
- board text added: "PA1"
- board text added: "PA10"
- board text added: "PA11"
- board text added: "PA12"
- board text added: "PA15"
- board text added: "PA2"
- board text added: "PA3"
- board text added: "PA4"
- board text added: "PA5"
- board text added: "PA6"
- board text added: "PA7"
- board text added: "PA8"
- board text added: "PA9"
- board text added: "PB0"
- board text added: "PB1"
- board text added: "PB10"
- board text added: "PB11"
- board text added: "PB12"
- board text added: "PB13"
- board text added: "PB14"
- board text added: "PB15"
- board text added: "PB2"
- board text added: "PB3"
- board text added: "PB4"
- board text added: "PB5"
- board text added: "PB6"
- board text added: "PB7"
- board text added: "PB8"
- board text added: "PB9"
- board text added: "PC13"
- board text added: "PF6"
- board text added: "PF7"
- board text added: "~NRST"
